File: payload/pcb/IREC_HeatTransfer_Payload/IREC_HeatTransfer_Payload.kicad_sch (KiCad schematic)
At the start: 37 parts, among them J1 XT60PW-M, J2 Screw_Terminal_01x02, J3 Screw_Terminal_01x02, J4 Screw_Terminal_01x02, J5 Screw_Terminal_01x02, SW1 SW_SPDT, U1 MAX31855KASA, U2 DS18B20, U3 DEV-16771, U4 MAX31855KASA, U5 MAX31855KASA, U7 AP63357

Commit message: updates
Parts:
- removed C12: 4.7uF, symbol Device:C
- added R6: 75, Resistor_SMD:R_0805_2012Metric_Pad1.20x1.40mm_HandSolder, symbol Device:R
- added R7, R8: 5, Resistor_SMD:R_0805_2012Metric_Pad1.20x1.40mm_HandSolder, symbol Device:R
- C1, C10, C2, C3, C4, C5, C6, C7, C8, C9: footprint (none) -> Capacitor_SMD:C_0805_2012Metric_Pad1.18x1.45mm_HandSolder
- C11: value 4.7uF -> 10uF; footprint (none) -> Capacitor_SMD:C_0805_2012Metric_Pad1.18x1.45mm_HandSolder
- L1: footprint (none) -> CustomFootprintLib:IND_SRN8040TA-6R8M
- R1: value 4k7 -> 4.7k; footprint (none) -> Resistor_SMD:R_0805_2012Metric_Pad1.20x1.40mm_HandSolder
- R2, R3: footprint (none) -> Resistor_SMD:R_0805_2012Metric_Pad1.20x1.40mm_HandSolder
- R4: value R -> 6.8k; footprint (none) -> Resistor_SMD:R_0805_2012Metric_Pad1.20x1.40mm_HandSolder
- R5: value R -> 16k; footprint (none) -> Resistor_SMD:R_0805_2012Metric_Pad1.20x1.40mm_HandSolder
- SW1: footprint (none) -> Button_Switch_SMD:SW_SPDT_CK_JS102011SAQN
- TC1, TC2, TC3: footprint (none) -> CustomFootprintLib:PCC-SMP-K
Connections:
- net +BATT: no longer SW1.1 (A)
- net EN: no longer R5.1
- net at D1.2 (RED): now also R6.2
- net at D1.3 (BLU): now also R7.2
- net at D1.4 (GRN): now also R8.2
- new net: R5.1, SW1.1 (A)
- new net BLU: R7.1
- new net GRN: R8.1
- new net RED: R6.1
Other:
- note added: "RGB LED"
- note added: "UVLO @ VCC ="
- moved on the sheet: C10, C11, C7, C8, C9, D1, J1, J5, L1, R2, R3, R4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

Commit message: Updates
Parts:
- removed D1: ~, symbol CustomComponents:Diffused_RGB_(tri-color)_LED_-_Common_Anode
- removed SW1: SW_SPDT, Button_Switch_SMD:SW_SPDT_CK_JS102011SAQN, symbol Switch:SW_SPDT
- added D1: OSRAM_LGR971-KN-1, Skyhawkson_Footprints:OSRAM_0805, symbol Skyhawkson-LEDs and Optoelectronics:OSRAM_LGR971-KN-1
- added D2: OSRAM_LSR976-NR-1, Skyhawkson_Footprints:OSRAM_0805, symbol Skyhawkson-LEDs and Optoelectronics:OSRAM_LSR976-NR-1
- added D3: ORANGE, symbol Device:LED
- added H1, H2, H3, H4: MountingHole_Pad, MountingHole:MountingHole_2.2mm_M2_Pad_Via, symbol Mechanical:MountingHole_Pad
- added R10: 100k, symbol Device:R
- added R9: 200k, symbol Device:R
- R4: value 6.8k -> 22k
- R5: value 16k -> 93.1k
- R6: value 75 -> R; footprint Resistor_SMD:R_0805_2012Metric_Pad1.20x1.40mm_HandSolder -> (none)
- R7, R8: value 5 -> R; footprint Resistor_SMD:R_0805_2012Metric_Pad1.20x1.40mm_HandSolder -> (none)
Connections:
- net BLU is gone; now on net LED_RED: R7.1
- net EN is gone; now on an unnamed net: R4.2, U7.2 (EN)
- net GRN is gone; now on net +5V: R8.1
- net +BATT: now also R9.1
- net GND: now also D1.C, D2.C, D3.1 (K), H1.1, H2.1, H3.1, H4.1, R10.2
- net VBAT_SENSE: now reaches U3.15 (A1)
- net VBAT_SENSE: now also R10.1, R9.2
- net LED_RED: now reaches U3.2 (OUT2)
- net LED_GREEN: now reaches U3.3 (LRCLK2)
- net LED_GREEN: now also R6.2
- net at R8.2: now also D3.2 (A)
- net at R7.2: now also D2.A
- net DS_DATA renamed TEMP_SENSE
- net RED: no longer names the net of R6.1
- net RED: now also D1.A
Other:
- note added: "2S LiPo (7.4V)"
- note added: "5V Voltage Regulator"
- note added: "6-32V VIN 3.5A OUT MAX"
- note added: "AP63357"
- note added: "Battery Connectors"
- note added: "Battery Voltage Range Single: 3V-4.2V Double: 6V-8.4V"
- note added: "DS18B20"
- note added: "Microcontroller"
- note added: "Status LEDs"
- note added: "TEENSY 4.1"
- note added: "UVLO Hi: 5.6V UVLO Lo: 5.18V"
- note added: "VIN: 3.6V-5.5V"
- note added: "Voltage Sensing"
- note removed: "5V Buck Converter"
- note removed: "Power Input"
- note removed: "RGB LED"
- note removed: "UVLO @ VCC ="
- moved on the sheet: C1, C10, C11, C2, C3, C4, C5, C6, C7, C8, C9, J1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

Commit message: updates to pcb
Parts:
- removed J5: Screw_Terminal_01x02, CustomFootprintLib:TERMBLOCK_OSTTE020104_3_5MM, symbol Connector:Screw_Terminal_01x02
- removed TC1, TC2, TC3: Thermocouple_Block, CustomFootprintLib:PCC-SMP-K, symbol Device:Thermocouple_Block
- added J5: S2B-PH-K-SLFSN, CONN_S2B-PH-K-S_JST, symbol CustomComponents:S2B-PH-K-SLFSN
- H1, H2, H3, H4: footprint MountingHole:MountingHole_2.2mm_M2_Pad_Via -> MountingHole:MountingHole_3.2mm_M3_Pad_Via
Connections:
- net +BATT: now also J5.1
- net GND: now also J5.2
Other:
- note added: "Voltage Range Single: 3V-4.2V Double: 6V-8.4V"
- note removed: "Battery Voltage Range Single: 3V-4.2V Double: 6V-8.4V"
- moved on the sheet: J3, J4

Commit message: updates
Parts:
- removed D3: ORANGE, symbol Device:LED
- removed J2, J3, J4: Screw_Terminal_01x02, CustomFootprintLib:TERMBLOCK_OSTTE020104_3_5MM, symbol Connector:Screw_Terminal_01x02
- removed J5: S2B-PH-K-SLFSN, CONN_S2B-PH-K-S_JST, symbol CustomComponents:S2B-PH-K-SLFSN
- removed R8: R, symbol Device:R
- added BT1: Battery_Cell, Battery:BatteryHolder_Keystone_3002_1x2032, symbol Device:Battery_Cell
- added J5: Screw_Terminal_01x06, CustomFootprintLib:TERMBLOCK_OSTTE060104, symbol Connector:Screw_Terminal_01x06
- added J6: Screw_Terminal_01x02, CustomFootprintLib:TERMBLOCK_OSTTE020104_3_5MM, symbol Connector:Screw_Terminal_01x02
- added SW1: SW_Push_SPDT, Button_Switch_SMD:SW_SPDT_CK_JS102011SAQN, symbol Switch:SW_Push_SPDT
- R6, R7: footprint (none) -> Resistor_SMD:R_0805_2012Metric_Pad1.20x1.40mm_HandSolder
- TP1, TP2, TP3: footprint (none) -> TestPoint:TestPoint_Keystone_5019_Minature
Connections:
- net +BATT: now also J6.1 (Pin_1)
- net GND: now also BT1.2 (-), J6.2 (Pin_2), SW1.3 (C)
- net EN: now reaches R4.2, U7.2 (EN)
- net EN: now also SW1.2 (B); no longer R5.1
- net VBAT_CR2032: now reaches U3.VBAT
- net VBAT_CR2032: now also BT1.1 (+)
- net +TC1: now reaches C4.1, U1.3 (T+)
- net +TC1: now also J5.5 (Pin_5)
- net -TC1: now reaches C4.2, U1.2 (T-)
- net -TC1: now also J5.6 (Pin_6)
- net -TC2: now reaches C5.2, U4.2 (T-)
- net -TC2: now also J5.4 (Pin_4)
- net +TC2: now reaches C5.1, U4.3 (T+)
- net +TC2: now also J5.3 (Pin_3)
- net -TC3: now reaches C6.2, U5.2 (T-)
- net -TC3: now also J5.2 (Pin_2)
- net +TC3: now reaches C6.1, U5.3 (T+)
- net +TC3: now also J5.1 (Pin_1)
- new net: R5.1, SW1.1 (A)
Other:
- moved on the sheet: R1, U2

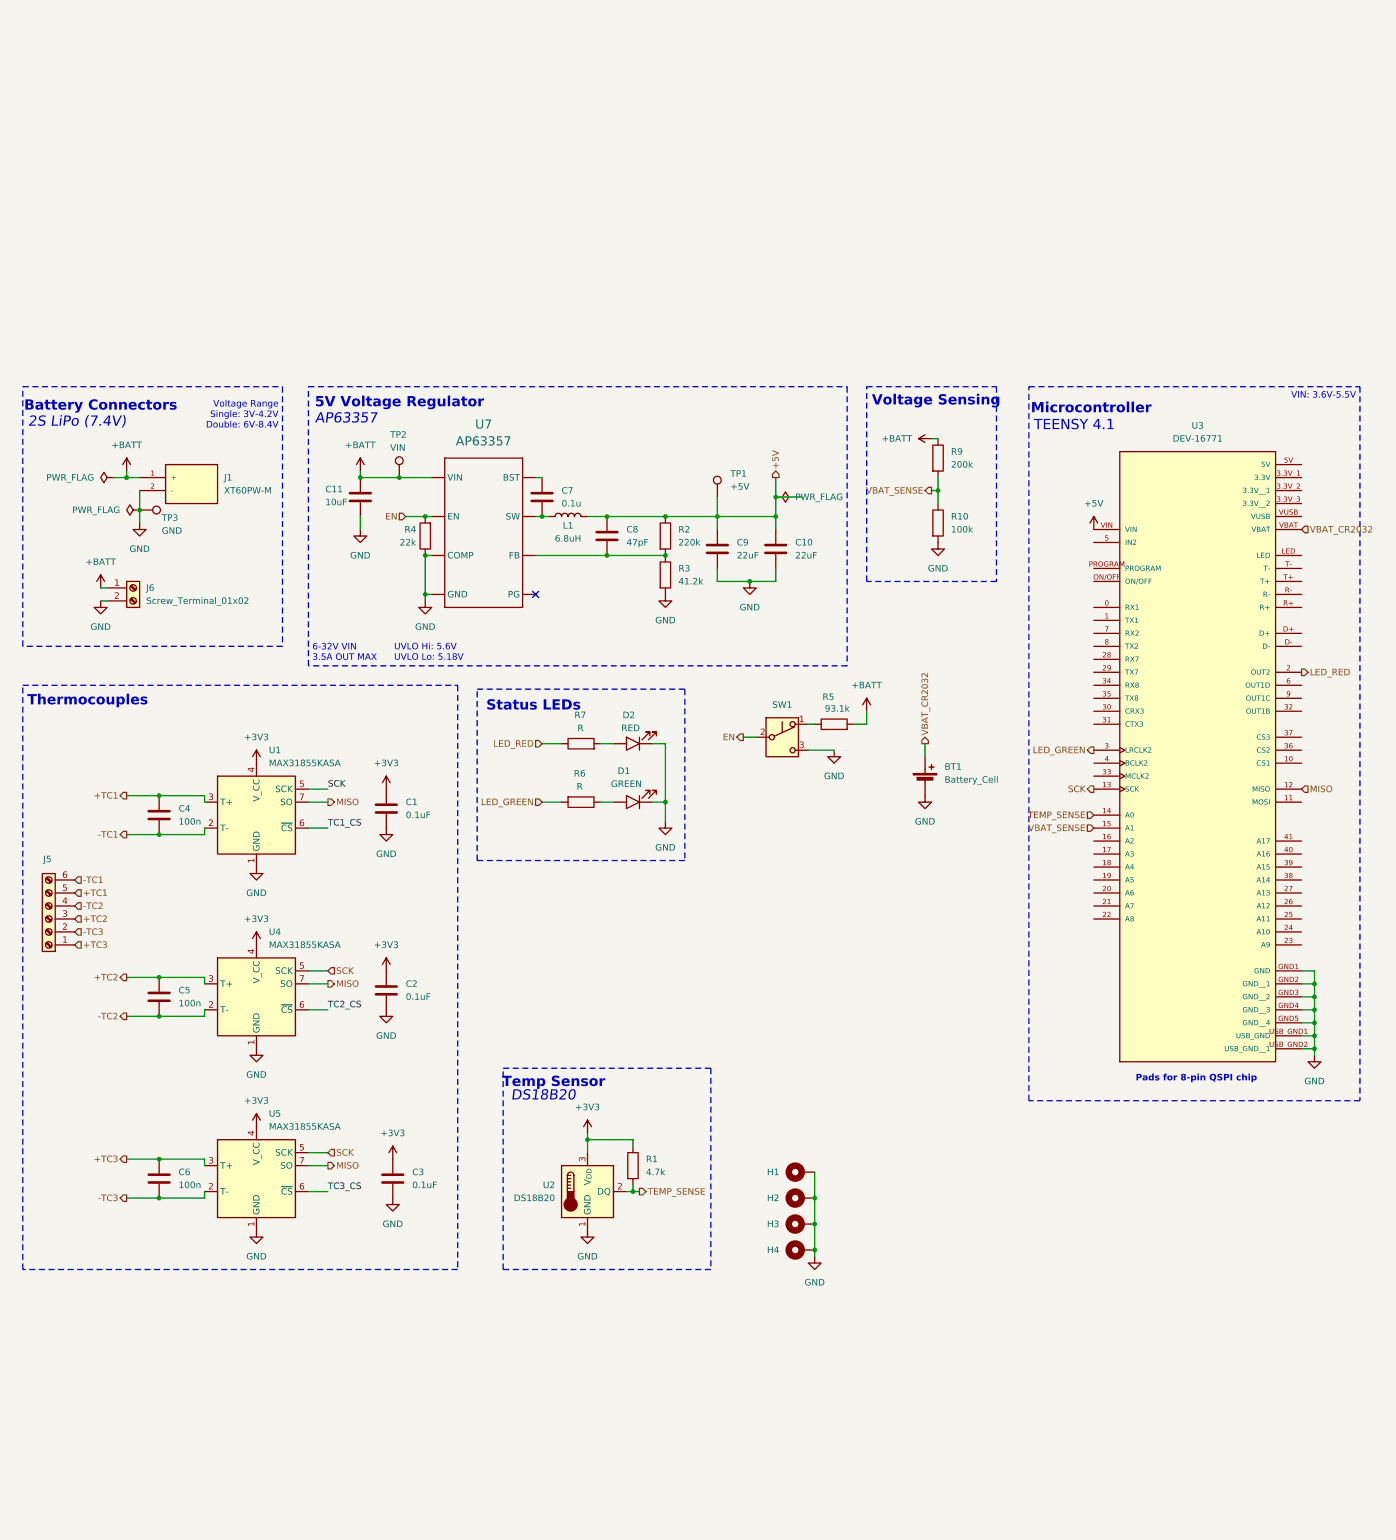
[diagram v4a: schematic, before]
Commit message: updates
continued buck layout
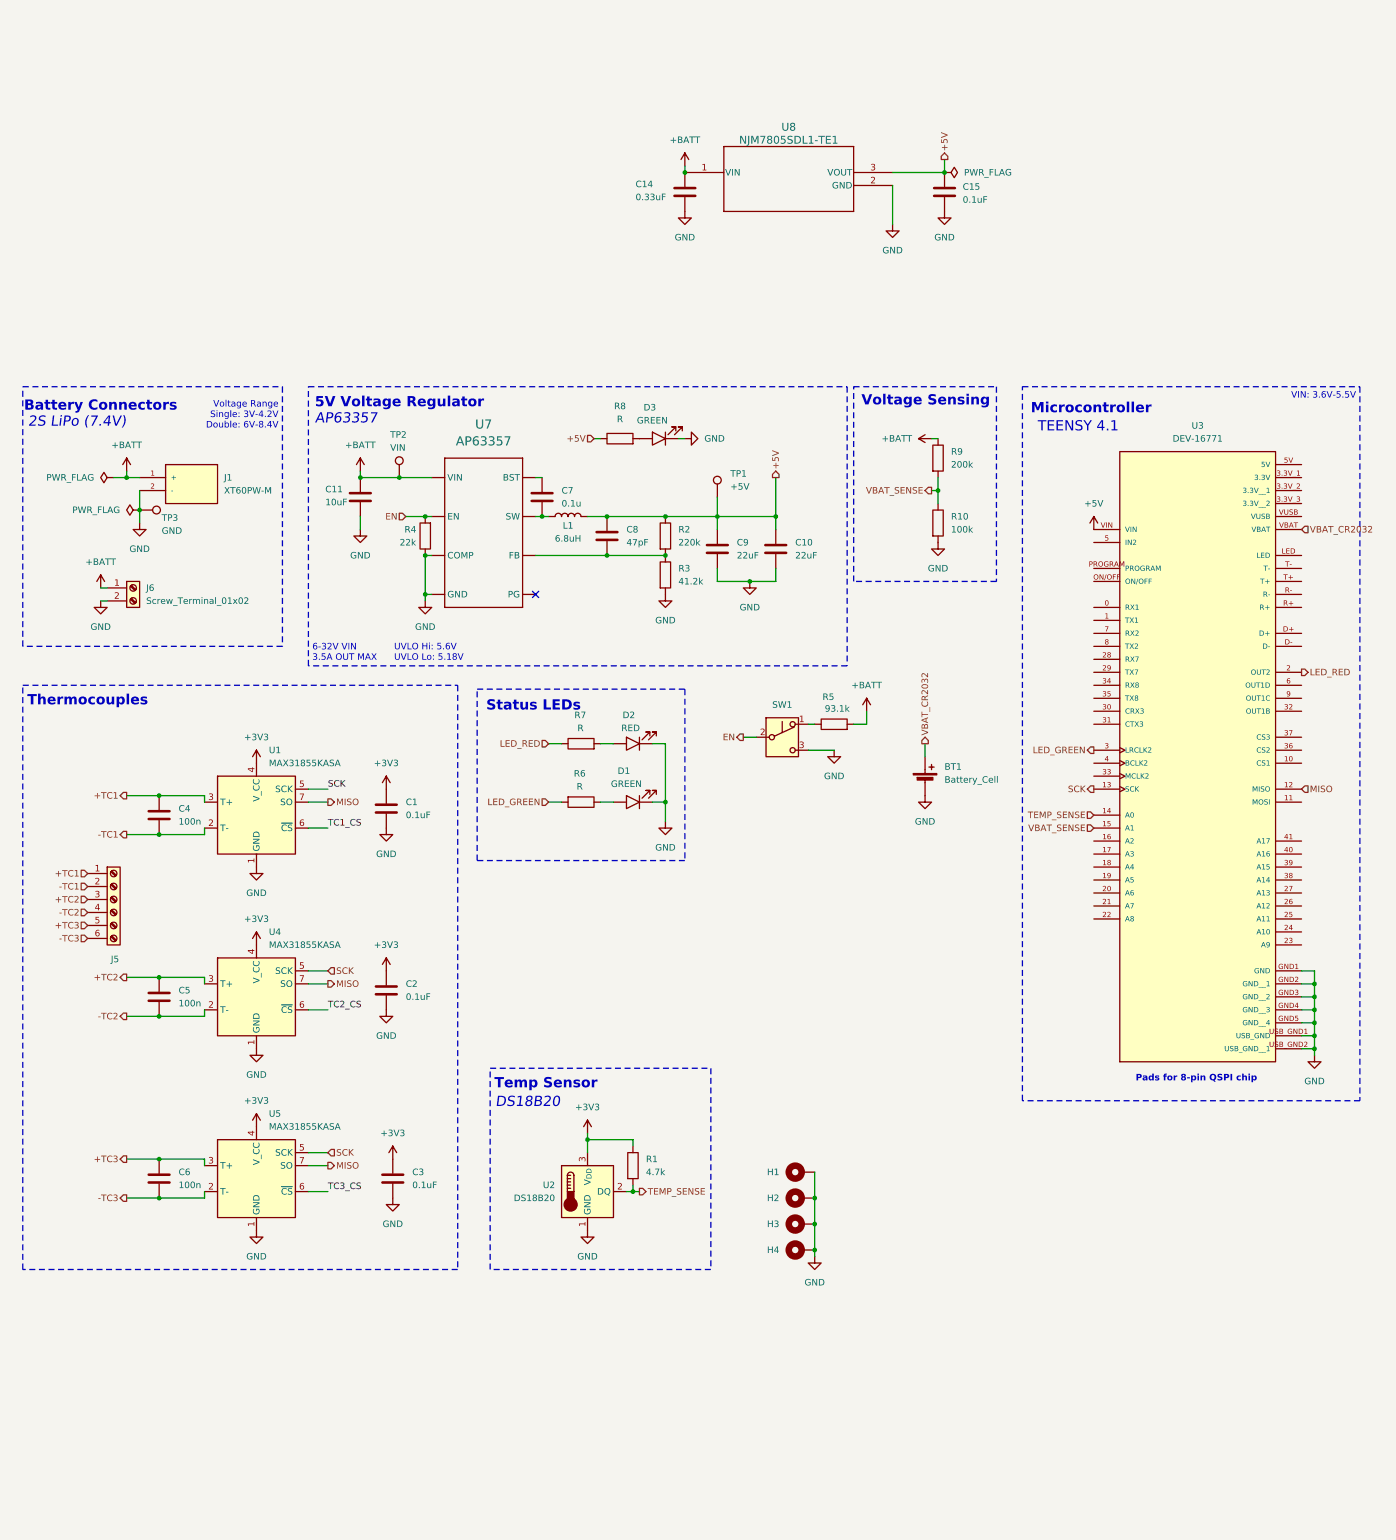
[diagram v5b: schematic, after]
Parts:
- added C14: 0.33uF, Capacitor_SMD:C_0805_2012Metric_Pad1.18x1.45mm_HandSolder, symbol Device:C
- added C15: 0.1uF, Capacitor_SMD:C_0805_2012Metric_Pad1.18x1.45mm_HandSolder, symbol Device:C
- added D3: OSRAM_LGR971-KN-1, Skyhawkson_Footprints:OSRAM_0805, symbol Skyhawkson-LEDs and Optoelectronics:OSRAM_LGR971-KN-1
- added R8: R, symbol Device:R
- added U8: NJM7805SDL1-TE1, CustomFootprintLib:TO-252-3-L1_NMD, symbol CustomComponents:NJM7805SDL1-TE1
- R10, R9: footprint (none) -> Resistor_SMD:R_0805_2012Metric_Pad1.20x1.40mm_HandSolder
- TP1, TP2: footprint TestPoint:TestPoint_Keystone_5019_Minature -> TestPoint:TestPoint_Loop_D2.54mm_Drill1.5mm_Beaded
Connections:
- net +5V: now also C15.1, R8.1, U8.3 (VOUT)
- net +BATT: now also C14.1, U8.1 (VIN)
- net +TC1: now also J5.1 (Pin_1); no longer J5.5 (Pin_5)
- net +TC3: now also J5.5 (Pin_5); no longer J5.1 (Pin_1)
- net -TC1: now also J5.2 (Pin_2); no longer J5.6 (Pin_6)
- net -TC3: now also J5.6 (Pin_6); no longer J5.2 (Pin_2)
- net GND: now also C14.2, C15.2, D3.C, U8.2 (GND)
- new net: D3.A, R8.2
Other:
- moved on the sheet: J5

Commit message: updates
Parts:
- removed D3: OSRAM_LGR971-KN-1, Skyhawkson_Footprints:OSRAM_0805, symbol Skyhawkson-LEDs and Optoelectronics:OSRAM_LGR971-KN-1
- removed R8: R, symbol Device:R
- TP1, TP2: footprint TestPoint:TestPoint_Loop_D2.54mm_Drill1.5mm_Beaded -> TestPoint:TestPoint_Pad_D1.0mm
- TP3: footprint TestPoint:TestPoint_Keystone_5019_Minature -> TestPoint:TestPoint_Pad_D1.0mm
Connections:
- net +5V: now also R7.1
- net LED_RED: no longer R7.1

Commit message: updates
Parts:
- removed J6: Screw_Terminal_01x02, CustomFootprintLib:TERMBLOCK_OSTTE020104_3_5MM, symbol Connector:Screw_Terminal_01x02
- removed R5: 93.1k, Resistor_SMD:R_0805_2012Metric_Pad1.20x1.40mm_HandSolder, symbol Device:R
- removed SW1: SW_Push_SPDT, Button_Switch_SMD:SW_SPDT_CK_JS102011SAQN, symbol Switch:SW_Push_SPDT
- added J4: Screw_Terminal_01x06, CustomFootprintLib:TERMBLOCK_OSTTE060104, symbol Connector:Screw_Terminal_01x06
- added JP1: Jumper_3_Open, Jumper:SolderJumper-3_P1.3mm_Open_RoundedPad1.0x1.5mm, symbol Jumper:Jumper_3_Open
- R4: value 22k -> R
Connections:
- net -TC2 is gone; now on net T-: C5.2, J5.4 (Pin_4), U4.2 (T-)
- net -TC3 is gone; now on net T-: C6.2, J5.6 (Pin_6), U5.2 (T-)
- net +3V3: now also U3.3.3V_1 (3.3V)
- net +BATT: now also J4.1 (Pin_1), J4.3 (Pin_3); no longer C11.1, C14.1, R9.1, TP2.1, U7.1 (VIN), U8.1 (VIN)
- net GND: now also J4.2 (Pin_2), J4.6 (Pin_6); no longer R4.1
- net LED_GREEN: now also R4.2
- net +TC1 renamed T1
- net +TC2 renamed T2
- net +TC3 renamed T3
- net -TC1 renamed T-
- net EN renamed V_BUCK
- net V_BUCK: now also C11.1, U7.1 (VIN), JP1.1 (A); no longer R4.2
- net TC1_CS renamed T1_CS
- net TC2_CS renamed T2_CS
- net TC3_CS renamed T3_CS
- new net: J4.5 (Pin_5), R4.1
- new net VCC: J4.4 (Pin_4), JP1.2 (C), R9.1, TP2.1
- new net V_LDO: C14.1, JP1.3 (B), U8.1 (VIN)
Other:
- note added: "5V Voltage Regulator (Alt.)"
- note added: "Battery Connector"
- note added: "CR2032"
- note added: "NJM7805SDL1-TE1"
- note added: "RTC Battery"
- note removed: "Battery Connectors"
- moved on the sheet: BT1, C1, C10, C11, C2, C3, C4, C5, C6, C7, C8, C9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

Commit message: upd
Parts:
- added J4: Conn_01x04, Connector_PinSocket_2.54mm:PinSocket_1x04_P2.54mm_Vertical, symbol Connector_Generic:Conn_01x04
- added J5: GPIO, Connector_PinSocket_2.54mm:PinSocket_1x04_P2.54mm_Vertical, symbol Connector_Generic:Conn_01x04
- added J6: SPI, Connector_PinSocket_2.54mm:PinSocket_1x03_P2.54mm_Vertical, symbol Connector_Generic:Conn_01x03
- added J7: I2C, Connector_PinSocket_2.54mm:PinSocket_1x02_P2.54mm_Vertical, symbol Connector_Generic:Conn_01x02
- renumbered C4 to C1, C14 to C10, C9 to C11, C10 to C12, C15 to C13, C5 to C2, C6 to C3, C11 to C4, C1 to C5, C2 to C6, C3 to C7, C7 to C8, C8 to C9, D2 to D1, D1 to D2, J5 to J1, J1 to J2, J4 to J3, R7 to R1, R6 to R2, R1 to R3, R2 to R4, R3 to R5, R4 to R6, R9 to R7, R10 to R8, TP3 to TP1, TP1 to TP2, TP2 to TP3, U4 to U2, U5 to U3, U7 to U4, U2 to U5, U8 to U6, U3 to U7
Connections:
- net +3V3: now also J4.2 (Pin_2)
- net +5V: now also J4.1 (Pin_1)
- net GND: now also J4.4 (Pin_4)
- net VCC: now also J4.3 (Pin_3)
- new net GPIO: J5.1 (Pin_1), J5.2 (Pin_2), J5.3 (Pin_3), J5.4 (Pin_4)
- new net I2C_SCL: J7.2 (Pin_2)
- new net I2C_SDA: J7.1 (Pin_1)
- new net SPI_MISO: J6.3 (Pin_3)
- new net SPI_MOSI: J6.2 (Pin_2)
- new net SPI_SCK: J6.1 (Pin_1)
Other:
- note added: "+"
- note added: "-"
- note added: "Main Battery"
- note added: "Main Switch"
- note added: "Power Option"
- note added: "Screw Terminals"
- note added: "Status LED"
- moved on the sheet: J3, JP1, R6, TP3
